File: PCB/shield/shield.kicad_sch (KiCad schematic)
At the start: 20 parts, among them J1 QTR-8A, J10 ESP32_left_m, J11 ESP32_right_m, J13 Conn_01x06, J14 Domino, J15 Domino, J2 QMC5883L, J3 Servo, J4 Domino, J5 Joystick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

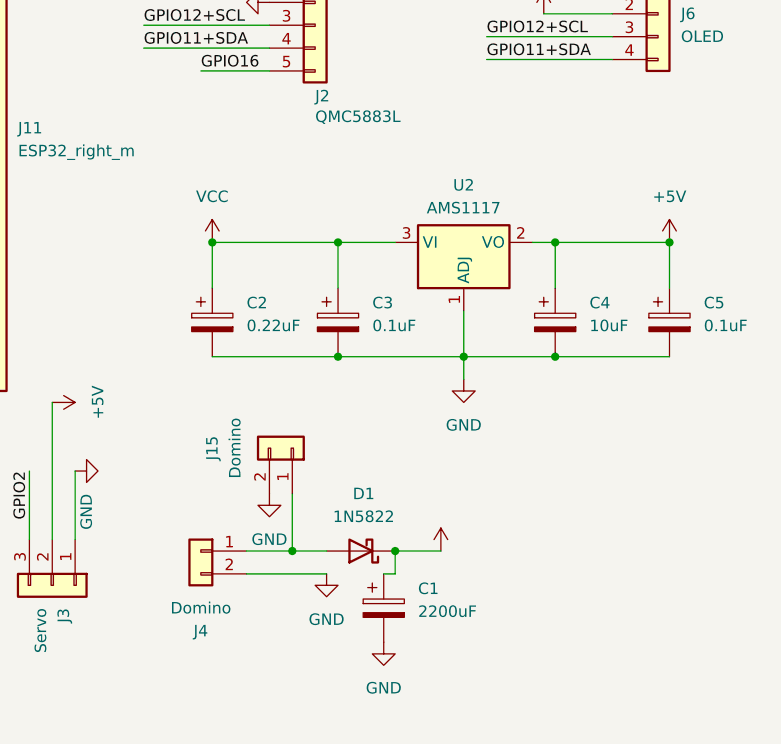
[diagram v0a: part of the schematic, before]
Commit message: feat: change AMS1117 to LM2596S
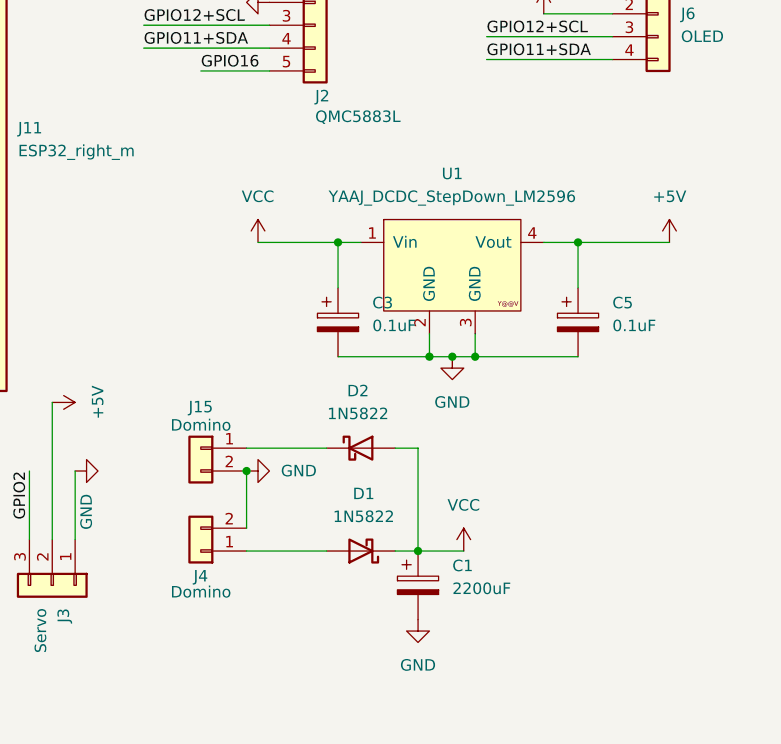
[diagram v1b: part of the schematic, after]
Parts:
- removed C2: 0.22uF, Capacitor_SMD:C_0805_2012Metric_Pad1.18x1.45mm_HandSolder, symbol Device:C_Polarized
- removed C4: 10uF, Capacitor_SMD:C_0805_2012Metric_Pad1.18x1.45mm_HandSolder, symbol Device:C_Polarized
- removed U2: AMS1117, Package_TO_SOT_SMD:SOT-223-3_TabPin2, symbol Regulator_Linear:AMS1117
- added D2: 1N5822, Diode_THT:D_DO-201AD_P15.24mm_Horizontal, symbol Diode:1N5822
- added U1: YAAJ_DCDC_StepDown_LM2596, KiCad:YAAJ_DCDC_StepDown_LM2596, symbol yaaj_dcdc_stepdown_lm2596:YAAJ_DCDC_StepDown_LM2596
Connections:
- net +5V: now also U1.4 (Vout)
- net GND: now also U1.2 (GND), U1.3 (GND)
- net VCC: now also D2.2 (A), U1.1 (Vin)
- net at D1.2 (A), J4.1 (Pin_1): no longer J15.1 (Pin_1)
- new net: D2.1 (K), J15.1 (Pin_1)
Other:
- moved on the sheet: C1, C5, J15, J4

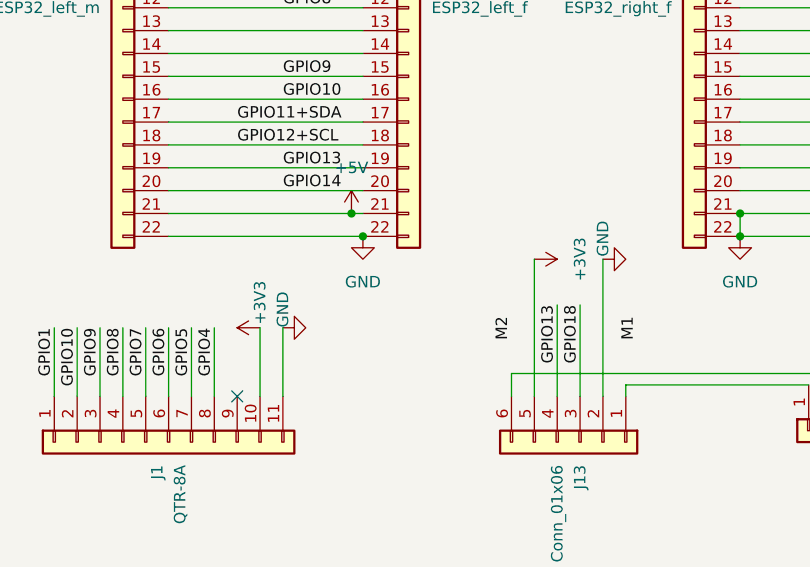
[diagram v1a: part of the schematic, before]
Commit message: feat: change pcb trace width; change sensors input voltage
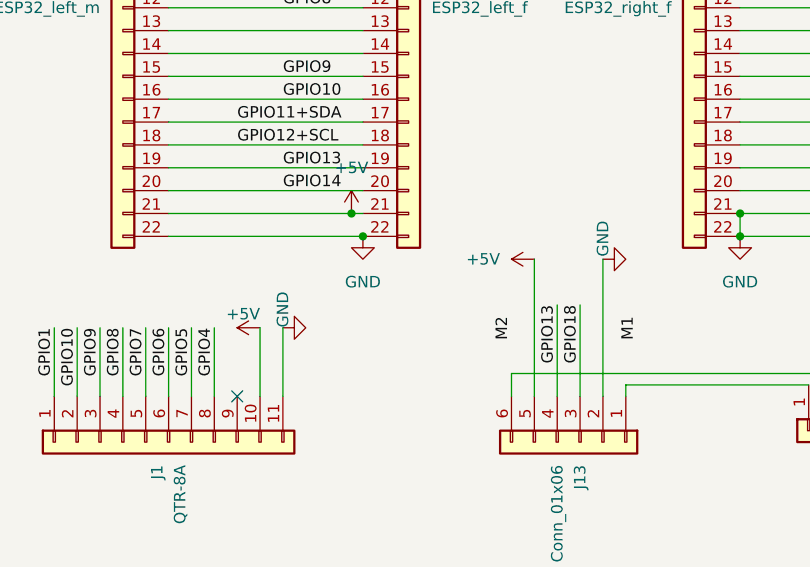
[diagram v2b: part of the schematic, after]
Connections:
- net +3V3: no longer J1.10 (Pin_10), J13.5 (Pin_5)
- net +5V: now also J1.10 (Pin_10), J13.5 (Pin_5)
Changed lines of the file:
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@@
 	)
 	(symbol
-		(lib_id "power:+3V3")
-		(at 83.82 135.89 90)
-		(mirror x)
-		(unit 1)
-		(exclude_from_sim no)
-		(in_bom yes)
-		(on_board yes)
-		(dnp no)
-		(property "Reference" "#PWR06"
-			(at 87.63 135.89 0)
-			(effects
-				(font
-					(size 1.27 1.27)
-				)
-				(hide yes)
-			)
-		)
-		(property "Value" "+3V3"
-			(at 83.82 133.096 0)
-			(effects
-				(font
-					(size 1.27 1.27)
-				)
-			)
-		)
-		(property "Footprint" ""
-			(at 83.82 135.89 0)
-			(effects
-				(font
-					(size 1.27 1.27)
-				)
-				(hide yes)
-			)
-		)
-		(property "Datasheet" ""
-			(at 83.82 135.89 0)
-			(effects
-				(font
-					(size 1.27 1.27)
-				)
-				(hide yes)
-			)
-		)
-		(property "Description" "Power symbol creates a global label with name \"+3V3\""
-			(at 83.82 135.89 0)
-			(effects
-				(font
-					(size 1.27 1.27)
-				)
-				(hide yes)
-			)
-		)
-		(pin "1"
-		)
-		(instances
-			(project ""
-				(path "/9a41b561-8e6b-4187-bd8f-1a6b5b887c54"
-					(reference "#PWR06")
-					(unit 1)
-				)
-			)
-		)
-	)
-	(symbol
 		(lib_id "Diode:1N5822")
 		(at 212.09 144.78 180)
@@
 	)
 	(symbol
-		(lib_id "power:+3V3")
-		(at 114.3 128.27 270)
-		(unit 1)
-		(exclude_from_sim no)
-		(in_bom yes)
-		(on_board yes)
-		(dnp no)
-		(fields_autoplaced yes)
-		(property "Reference" "#PWR020"
-			(at 110.49 128.27 0)
-			(effects
-				(font
-					(size 1.27 1.27)
-				)
-				(hide yes)
-			)
-		)
-		(property "Value" "+3V3"
-			(at 119.38 128.27 0)
-			(effects
-				(font
-					(size 1.27 1.27)
-				)
-			)
-		)
-		(property "Footprint" ""
-			(at 114.3 128.27 0)
-			(effects
-				(font
-					(size 1.27 1.27)
-				)
-				(hide yes)
-			)
-		)
-		(property "Datasheet" ""
-			(at 114.3 128.27 0)
-			(effects
-				(font
-					(size 1.27 1.27)
-				)
-				(hide yes)
-			)
-		)
-		(property "Description" "Power symbol creates a global label with name \"+3V3\""
-			(at 114.3 128.27 0)
-			(effects
-				(font
-					(size 1.27 1.27)
-				)
-				(hide yes)
-			)
-		)
-		(pin "1"
-		)
-		(instances
-			(project ""
-				(path "/9a41b561-8e6b-4187-bd8f-1a6b5b887c54"
-					(reference "#PWR020")
-					(unit 1)
-				)
-			)
-		)
-	)
-	(symbol
 		(lib_id "Connector_Generic:Conn_01x02")
 		(at 194.31 144.78 180)
@@
 	)
 	(symbol
+		(lib_id "power:+5V")
+		(at 114.3 128.27 90)
+		(unit 1)
+		(exclude_from_sim no)
+		(in_bom yes)
+		(on_board yes)
+		(dnp no)
+		(fields_autoplaced yes)
+		(property "Reference" "#PWR020"
+			(at 118.11 128.27 0)
+			(effects
+				(font
+					(size 1.27 1.27)
+				)
+				(hide yes)
+			)
+		)
+		(property "Value" "+5V"
+			(at 110.49 128.2699 90)
+			(effects
+				(font
+					(size 1.27 1.27)
+				)
+				(justify left)
+			)
+		)
+		(property "Footprint" ""
+			(at 114.3 128.27 0)
+			(effects
+				(font
+					(size 1.27 1.27)
+				)
+				(hide yes)
+			)
+		)
+		(property "Datasheet" ""
+			(at 114.3 128.27 0)
+			(effects
+				(font
+					(size 1.27 1.27)
+				)
+				(hide yes)
+			)
+		)
+		(property "Description" "Power symbol creates a global label with name \"+5V\""
+			(at 114.3 128.27 0)
+			(effects
+				(font
+					(size 1.27 1.27)
+				)
+				(hide yes)
+			)
+		)
+		(pin "1"
+		)
+		(instances
+			(project "shield"
+				(path "/9a41b561-8e6b-4187-bd8f-1a6b5b887c54"
+					(reference "#PWR020")
+					(unit 1)
+				)
+			)
+		)
+	)
+	(symbol
 		(lib_id "Device:C_Polarized")
 		(at 209.55 119.38 0)
@@
 					(unit 1)
 				)
+			)
+		)
+	)
+	(symbol
+		(lib_id "power:+5V")
+		(at 83.82 135.89 90)
+		(unit 1)
+		(exclude_from_sim no)
+		(in_bom yes)
+		(on_board yes)
+		(dnp no)
+		(property "Reference" "#PWR06"
+			(at 87.63 135.89 0)
+			(effects
+				(font
+					(size 1.27 1.27)
+				)
+				(hide yes)
+			)
+		)
+		(property "Value" "+5V"
+			(at 83.82 134.366 90)
+			(effects
+				(font
+					(size 1.27 1.27)
+				)
+				(justify left)
+			)
+		)
+		(property "Footprint" ""
+			(at 83.82 135.89 0)
+			(effects
+				(font
+					(size 1.27 1.27)
+				)
+				(hide yes)
+			)
+		)
+		(property "Datasheet" ""
+			(at 83.82 135.89 0)
+			(effects
+				(font
+					(size 1.27 1.27)
+				)
+				(hide yes)
+			)
+		)
+		(property "Description" "Power symbol creates a global label with name \"+5V\""
+			(at 83.82 135.89 0)
+			(effects
+				(font
+					(size 1.27 1.27)
+				)
+				(hide yes)
+			)
+		)
+		(pin "1"
+		)
+		(instances
+			(project "shield"
+				(path "/9a41b561-8e6b-4187-bd8f-1a6b5b887c54"
+					(reference "#PWR06")
+					(unit 1)
+				)

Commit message: wip: commit to change workplace
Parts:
- removed J10: ESP32_left_m, Connector_PinHeader_2.54mm:PinHeader_1x22_P2.54mm_Vertical, symbol Connector_Generic:Conn_01x22
- removed J11: ESP32_right_m, Connector_PinHeader_2.54mm:PinHeader_1x22_P2.54mm_Vertical, symbol Connector_Generic:Conn_01x22
- removed J8: ESP32_left_f, Connector_PinSocket_2.54mm:PinSocket_1x22_P2.54mm_Vertical, symbol Connector_Generic:Conn_01x22
- removed J9: ESP32_right_f, Connector_PinSocket_2.54mm:PinSocket_1x22_P2.54mm_Vertical, symbol Connector_Generic:Conn_01x22
- added D3: LED, symbol Device:LED
- added J7: L298N, Connector_JST:JST_XH_B3B-XH-A_1x03_P2.50mm_Vertical, symbol Connector_Generic:Conn_01x03
- added J8: USB_A, symbol Connector:USB_A
- added J9: Barrel_Jack, symbol Connector:Barrel_Jack
- added R1: R, symbol Device:R
- added SW1: SW_SPST, symbol Switch:SW_SPST
- added U2: ESP32-S3-DevKitC, PCM_Espressif:ESP32-S3-DevKitC, symbol PCM_Espressif:ESP32-S3-DevKitC
- C3, C5: footprint Capacitor_SMD:C_0805_2012Metric_Pad1.18x1.45mm_HandSolder -> Capacitor_THT:CP_Radial_D5.0mm_P2.50mm
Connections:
- net GPIO11+SDA is gone; now on net GPIO16: J2.4 (Pin_4), J6.4 (Pin_4)
- net GPIO12+SCL is gone; now on net GPIO15: J2.3 (Pin_3), J6.3 (Pin_3)
- net +3V3: now also U2.1 (3V3), U2.2 (3V3)
- net +5V: now also U2.21 (5V)
- net GND: now also D3.1 (K), J8.4 (GND), J8.5 (Shield), J9.2, U2.22 (GND), U2.23 (GND), U2.24 (GND), U2.44 (GND)
- net GPIO1: now also J5.4 (Pin_4), U2.41 (GPIO1/ADC1_CH0); no longer J1.1 (Pin_1)
- net GPIO10: now also J1.8 (Pin_8), U2.16 (GPIO10/ADC1_CH9); no longer J1.2 (Pin_2)
- net GPIO13: now also J7.2 (Pin_2), U2.19 (GPIO13/ADC2_CH2); no longer J13.4 (Pin_4)
- net GPIO14: now also J7.1 (Pin_1), U2.20 (GPIO14/ADC2_CH3); no longer J5.3 (Pin_3)
- net GPIO15: now also U2.8 (GPIO15/ADC2_CH4/32K_P); no longer J5.5 (Pin_5)
- net GPIO16: now also U2.9 (GPIO16/ADC2_CH5/32K_N); no longer J2.5 (Pin_5)
- net GPIO17: now also J13.3 (Pin_3), U2.10 (GPIO17/ADC2_CH6); no longer J5.4 (Pin_4)
- net GPIO18: now also J13.4 (Pin_4), U2.11 (GPIO18/ADC2_CH7); no longer J13.3 (Pin_3)
- net GPIO2: now also J5.3 (Pin_3), U2.40 (GPIO2/ADC1_CH1); no longer J3.3 (Pin_3)
- net GPIO4: now also J1.1 (Pin_1), U2.4 (GPIO4/ADC1_CH3); no longer J1.8 (Pin_8)
- net GPIO5: now also J1.2 (Pin_2), U2.5 (GPIO5/ADC1_CH4); no longer J1.7 (Pin_7)
- net GPIO6: now also J1.3 (Pin_3), U2.6 (GPIO6/ADC1_CH5); no longer J1.6 (Pin_6)
- net GPIO7: now also J1.4 (Pin_4), U2.7 (GPIO7/ADC1_CH6); no longer J1.5 (Pin_5)
- net GPIO8: now also J1.5 (Pin_5), U2.12 (GPIO8/ADC1_CH7); no longer J1.4 (Pin_4)
- net GPIO9: now also J1.7 (Pin_7), U2.15 (GPIO9/ADC1_CH8); no longer J1.3 (Pin_3)
- net M1: now also J13.1 (Pin_1), J14.1 (Pin_1)
- net M2: now also J13.6 (Pin_6), J14.2 (Pin_2)
- net VCC: now also D1.2 (A), D2.1 (K); no longer D1.1 (K), D2.2 (A)
- net at J4.1 (Pin_1): now also D2.2 (A); no longer D1.2 (A)
- net at J15.1 (Pin_1): now also D1.1 (K); no longer D2.1 (K)
- new net: J8.1 (VBUS), R1.1, SW1.1 (A)
- new net: J9.1, SW1.2 (B)
- new net: D3.2 (A), R1.2
- new net GPIO11: J3.3 (Pin_3), U2.17 (GPIO11/ADC2_CH0)
- new net GPIO12: J5.5 (Pin_5), U2.18 (GPIO12/ADC2_CH1)
- new net GPIO21: J7.3 (Pin_3), U2.27 (GPIO21)
- new net GPIO3: J1.6 (Pin_6), U2.13 (GPIO3/ADC1_CH2)
- no-connect marks 1 -> 2
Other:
- moved on the sheet: C1, D1, D2, J1, J13, J14, J15, J2, J3, J4, J5, J6

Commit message: wip: commit to change workspace
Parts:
- removed D1: 1N5822, Diode_THT:D_DO-201AD_P15.24mm_Horizontal, symbol Diode:1N5822
- removed D3: LED, symbol Device:LED
- removed J8: USB_A, symbol Connector:USB_A
- removed J9: Barrel_Jack, symbol Connector:Barrel_Jack
- added D1: BZT52C5V1, Diode_SMD:D_SOD-123, symbol Device:D_Zener
- added Q1: SI2301DS, Package_TO_SOT_SMD:SOT-23-3, symbol Device:Q_PMOS
- R1: value R -> 10k; footprint (none) -> Resistor_SMD:R_0603_1608Metric_Pad0.98x0.95mm_HandSolder
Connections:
- net GND: now also R1.2, SW1.2 (B); no longer J4.2 (Pin_2)
- net VCC: now also J15.1 (Pin_1); no longer C1.1
- net at R1.1: now also D1.2 (A), Q1.G; no longer SW1.1 (A)
- net at D2.2 (A): now also D1.1 (K), Q1.S; no longer J4.1 (Pin_1)
- new net: C1.1, J4.1 (Pin_1), Q1.D
- new net: J4.2 (Pin_2), SW1.1 (A)
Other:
- moved on the sheet: C1, J15, J4
